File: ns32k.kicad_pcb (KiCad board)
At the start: 4 copper layers, 125.4 x 90.5 mm, 96 parts, among them J1 Conn_01x02_Pin, J2 3V3 Serial, J3 USB_C_USB2.0_16P, U1 NS32201, U10 74AHC373, U11 74AHC373, U12 74AHC138, U13 AS6C6416-55, U14 MT29F8G08ABACA, U15 MX29LV040C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

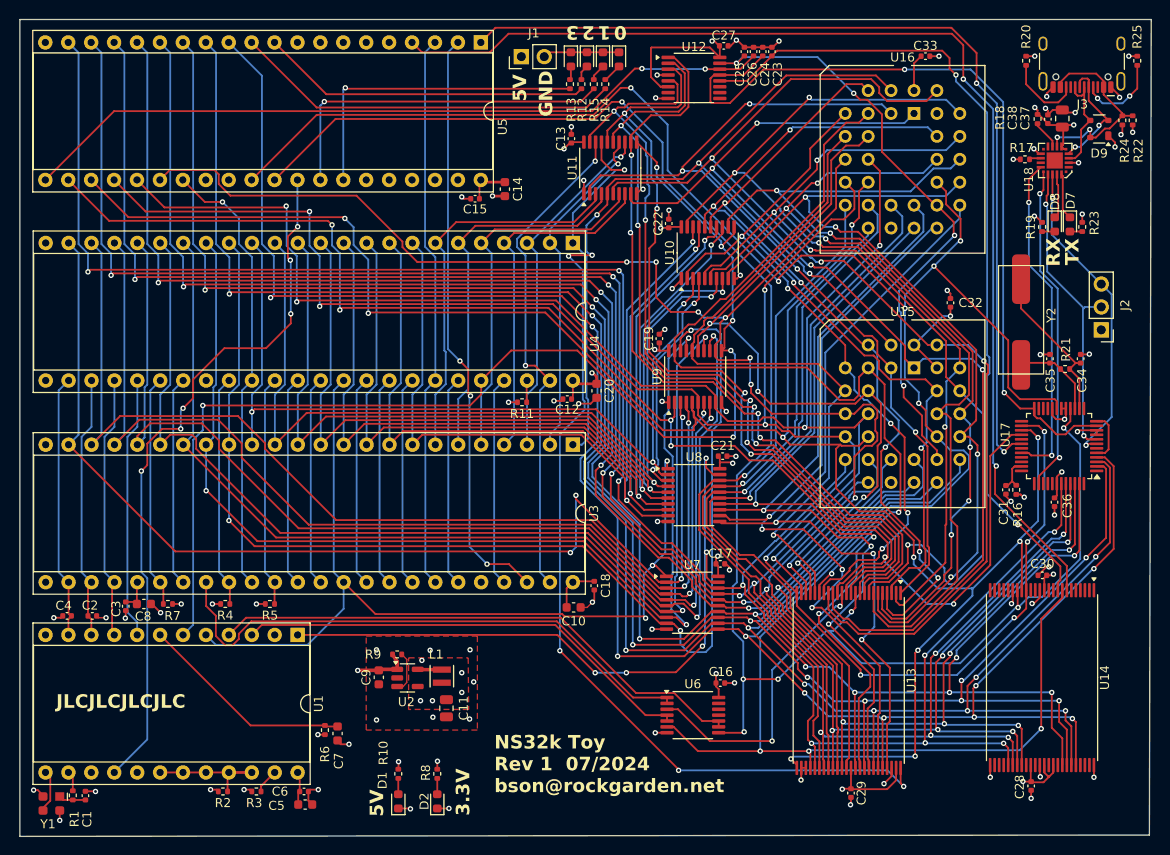
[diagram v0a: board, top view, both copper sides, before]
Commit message: add ICU int ack decoding
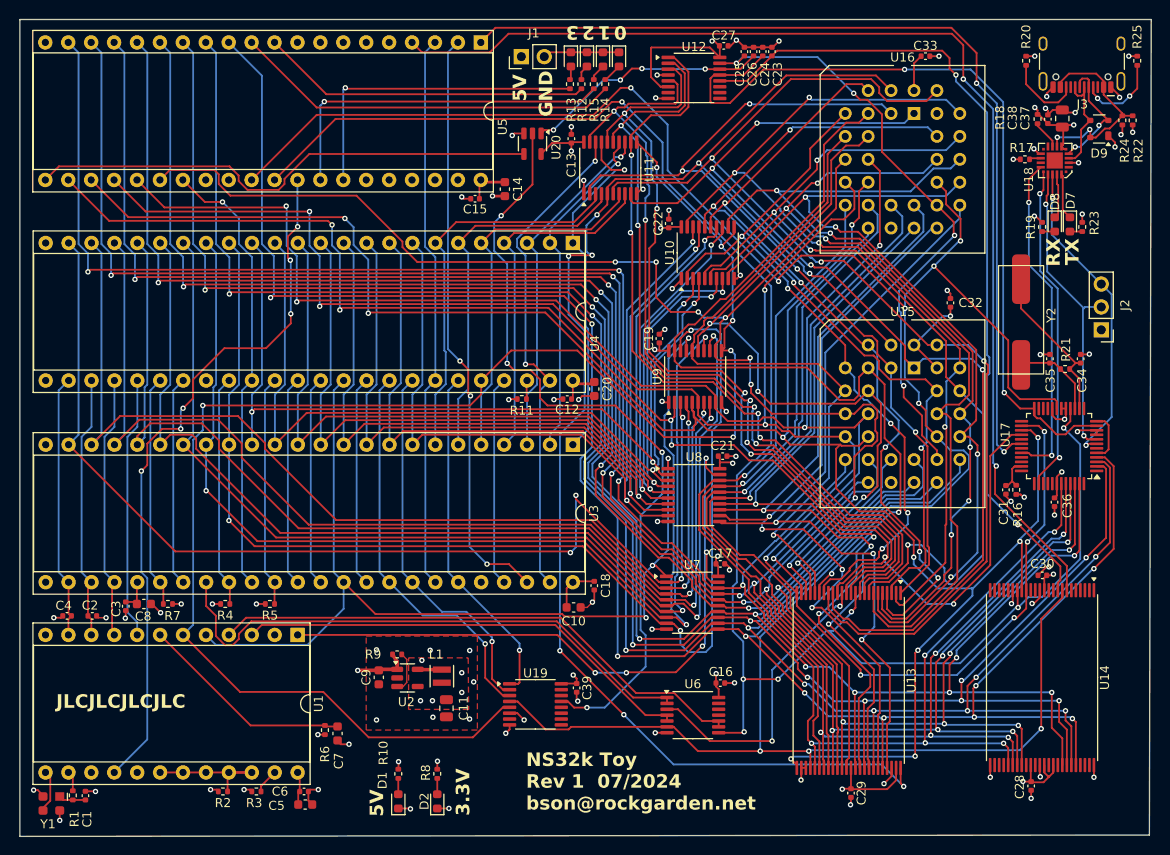
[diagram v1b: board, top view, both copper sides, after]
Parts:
- added C39: 0.1µF, Capacitor_SMD:C_0402_1005Metric, F.Cu at (113.4, 104.3)
- added U19: 74AHC138, Package_SO:TSSOP-16_4.4x5mm_P0.65mm, F.Cu at (108.8, 106.1)
- added U20: 74AHC1G08, Package_TO_SOT_SMD:SOT-23-5, F.Cu at (108.5, 44.0)
- U6: value 74LS08 -> 74AHC08
- moved R11 0.36 mm to (107.3, 72.3)
- moved C20 0.33 mm to (115.3, 71.2)
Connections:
- U5 pad 21: /~{ICU} -> Net-(U5B-~{CS})
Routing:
- net Net-(U19-O2): track 0.00 -> 86.8 mm, vias 0 -> 4
- net Net-(U5B-~{CS}): track 0.00 -> 57.1 mm
- net /~{ICU}: track 84.2 -> 27.2 mm, vias 2 -> 4
- net /~{PAV}: track 134.2 -> 176.5 mm
- net /ST3: track 23.3 -> 44.0 mm, vias 0 -> 1
- net /~{RD33}: track 260.8 -> 279.6 mm
- net /ST2: track 23.3 -> 41.7 mm, vias 0 -> 1
- net /ST0: track 23.3 -> 38.4 mm, vias 0 -> 1
- net +3V3: track 84.7 -> 93.2 mm, vias 26 -> 28
- net GND: track 92.9 -> 95.6 mm, vias 68 -> 71
- net +5V: track 33.2 -> 31.2 mm, vias 11 -> 10
- net /A22: track 40.4 -> 39.8 mm
- net /~{DDIN}: track 100.2 -> 100.8 mm

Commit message: move ICU# delay to after decode
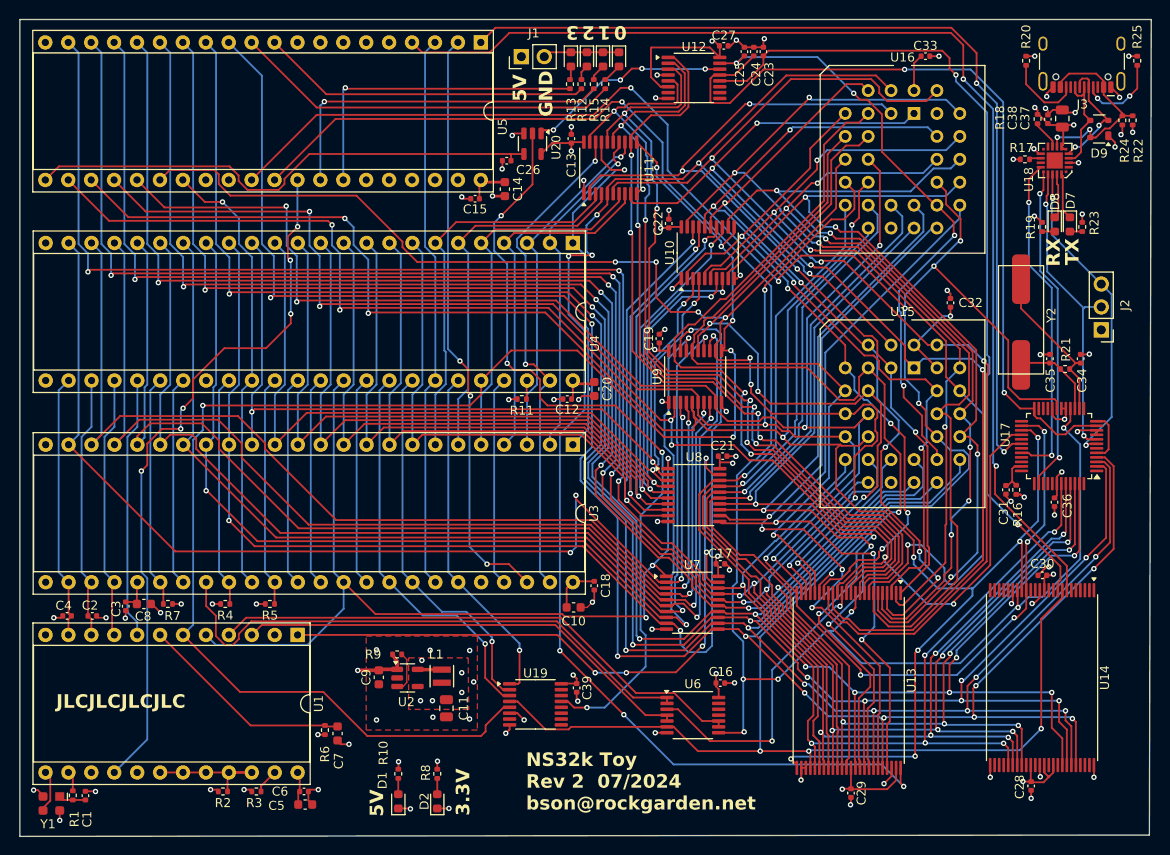
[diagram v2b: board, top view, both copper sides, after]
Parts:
- moved C26 29.9 mm to (105.6, 45.9), turned to 180 degrees
- moved C24 0.99 mm to (133.0, 33.8)
- moved C23 0.94 mm to (134.1, 33.8)
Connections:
- C26 pad 1: /~{ICU} -> Net-(U5B-~{CS})
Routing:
- net /~{ICU}: track 27.2 -> 22.8 mm
- net /~{SER_CS}: track 90.2 -> 89.2 mm
- net Net-(U5B-~{CS}): track 57.1 -> 57.9 mm
- net /~{NAND}: track 91.6 -> 92.2 mm
- net GND: vias 71 -> 72
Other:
- board text added: "NS32k Toy Rev 2 07/2024 bson@rockgarden.net"
- board text removed: "NS32k Toy Rev 1 07/2024 bson@rockgarden.net"

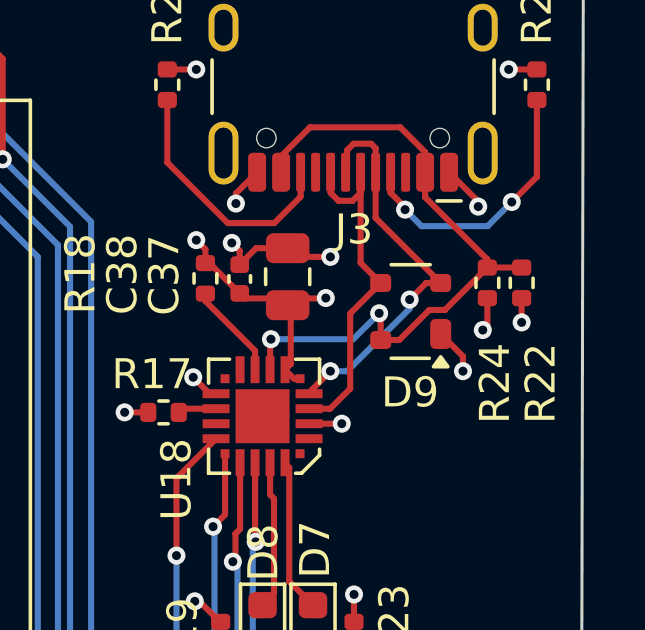
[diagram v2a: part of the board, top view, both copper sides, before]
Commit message: fix VUSB bug
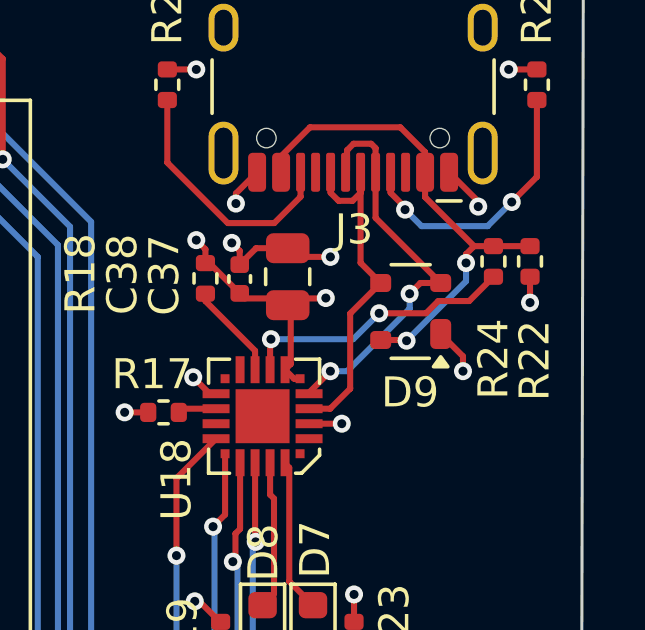
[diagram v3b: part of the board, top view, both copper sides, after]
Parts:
- R22: value 47k -> 47.5k
- R24: value 24k -> 22.1k
- moved R22 0.77 mm to (175.3, 40.7)
- moved R24 0.74 mm to (174.0, 40.7), turned to -90 degrees
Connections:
- D9 pad 4: Net-(U18-VBUS) -> Net-(D9-K-Pad4)
- J3 pad A4: Net-(U18-VBUS) -> Net-(D9-K-Pad4)
- J3 pad A9: Net-(U18-VBUS) -> Net-(D9-K-Pad4)
- J3 pad B4: Net-(U18-VBUS) -> Net-(D9-K-Pad4)
- J3 pad B9: Net-(U18-VBUS) -> Net-(D9-K-Pad4)
- R22 pad 1: Net-(U18-VBUS) -> Net-(D9-K-Pad4)
- R24 pad 1: +3V3 -> Net-(D9-K-Pad4)
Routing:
- net Net-(D9-K-Pad4): track 0.00 -> 16.2 mm, vias 0 -> 2
- net Net-(U18-VBUS): track 21.9 -> 9.31 mm
- net +3V3: track 93.2 -> 92.1 mm, vias 28 -> 27

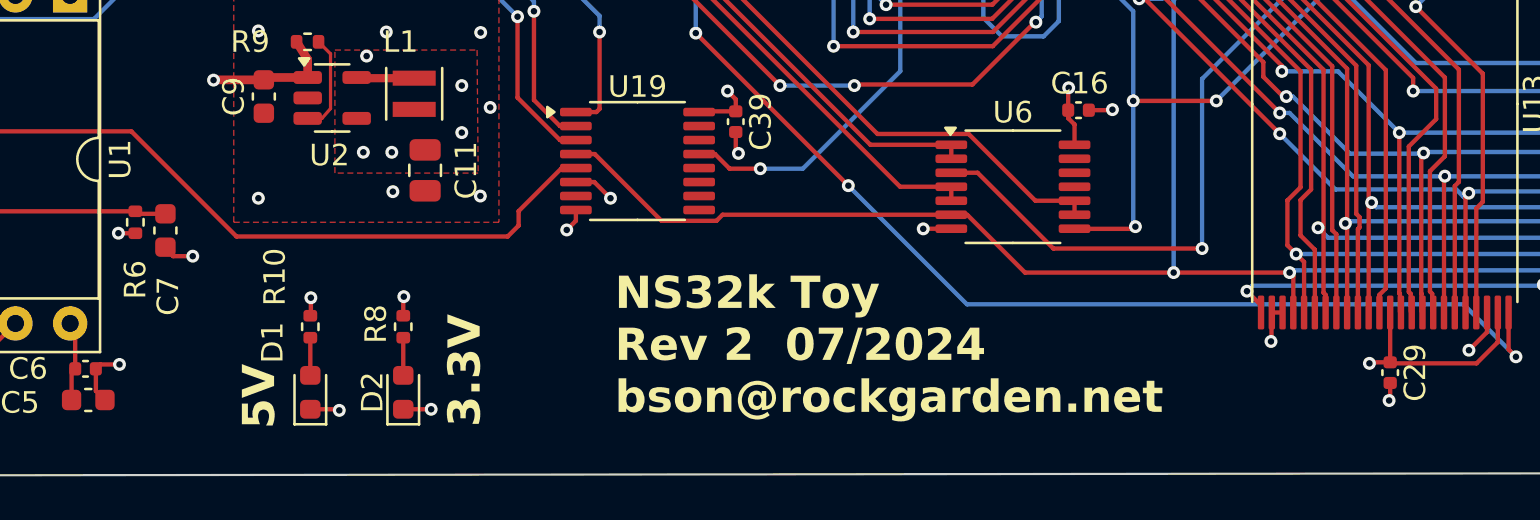
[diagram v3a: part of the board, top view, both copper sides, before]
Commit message: add reset button
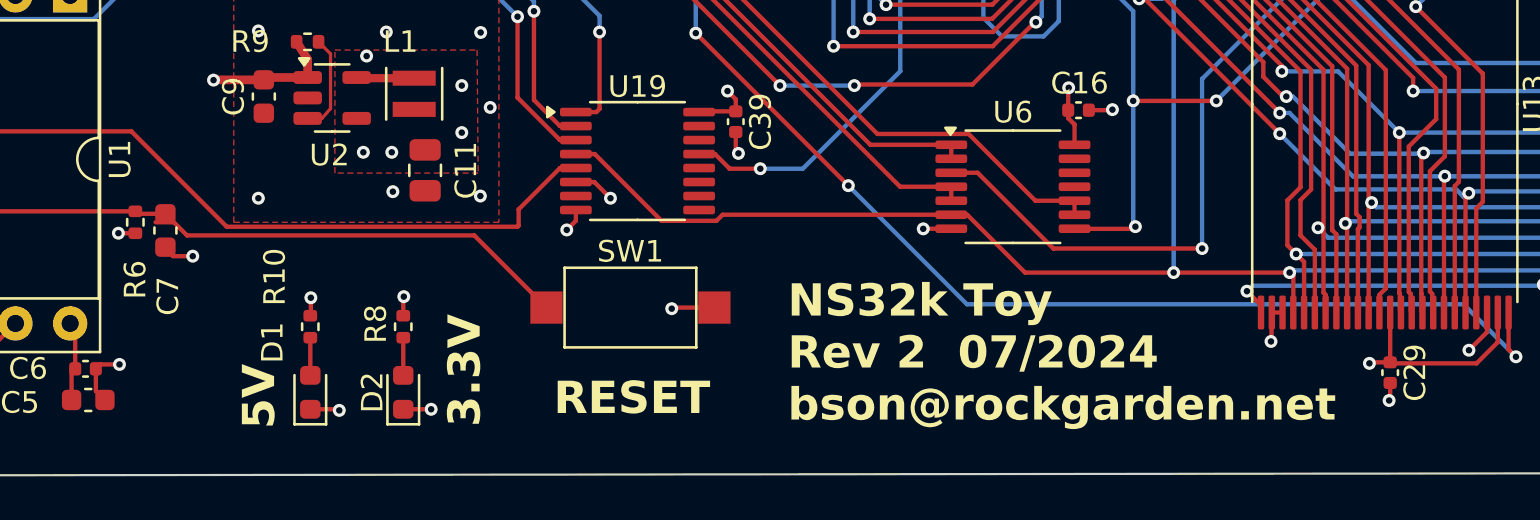
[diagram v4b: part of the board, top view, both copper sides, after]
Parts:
- added SW1: RESET, Button_Switch_SMD:SW_SPST_CK_RS282G05A3, F.Cu at (108.5, 112.9)
- J1: value Conn_01x02_Pin -> +5V SUPPLY
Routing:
- net Net-(U1B-~{RSTI}): track 23.7 -> 43.5 mm
- net GND: track 95.6 -> 97.6 mm, vias 72 -> 73
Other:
- board text added: "RESET"

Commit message: cleanups, DRC
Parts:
- added R26: 30k, Resistor_SMD:R_0402_1005Metric, B.Cu at (84.4, 35.9)
- added R27: 30k, Resistor_SMD:R_0402_1005Metric, F.Cu at (92.5, 50.5)
- added R28: 30k, Resistor_SMD:R_0402_1005Metric, B.Cu at (87.6, 35.9)
- added R29: 30k, Resistor_SMD:R_0402_1005Metric, F.Cu at (95.2, 50.5)
- added SW2: SW_DIP_x04, Button_Switch_SMD:SW_DIP_SPSTx04_Slide_Copal_CHS-04B_W7.62mm_P1.27mm, B.Cu at (75.9, 40.8)
- J3, R20, R25: moved to B.Cu
- moved R20 12.4 mm to (175.4, 37.2)
- moved R25 12.4 mm to (163.3, 37.2)
- moved Y1 5.48 mm to (54.7, 111.6), turned to 90 degrees
- moved C7 4.87 mm to (91.2, 111.6)
- moved R6 4.87 mm to (89.8, 111.2)
- moved U1 3.94 mm to (86.4, 98.4)
- moved D1 3.91 mm to (95.2, 113.3), turned to -90 degrees
- moved D2 3.90 mm to (99.5, 113.3), turned to -90 degrees
- moved C6 3.70 mm to (86.9, 115.9)
- moved C1 3.43 mm to (55.6, 115.4), turned to 0 degrees
- moved R1 2.90 mm to (55.6, 114.0), turned to 0 degrees
- moved C5 1.28 mm to (84.0, 116.2), turned to 180 degrees
- moved C29 1.25 mm to (143.3, 114.8), turned to 180 degrees
- moved C2 0.88 mm to (60.5, 96.0)
- moved D9 0.83 mm to (170.8, 41.7), turned to -90 degrees
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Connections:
- U5 pad 35: unconnected-(U5B-IR5-Pad35) -> Net-(U5B-IR5)
- U5 pad 36: unconnected-(U5B-IR7-Pad36) -> Net-(U5B-IR7)
- U5 pad 8: unconnected-(U5B-IR6-Pad8) -> Net-(U5B-IR6)
- U5 pad 9: unconnected-(U5B-IR4-Pad9) -> Net-(U5B-IR4)
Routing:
- net Net-(U5B-IR5): track 0.00 -> 20.6 mm
- net Net-(U5B-IR6): track 0.00 -> 20.5 mm
- net Net-(U5B-IR7): track 0.00 -> 18.4 mm, vias 0 -> 1
- net GND: track 97.6 -> 115.0 mm, vias 73 -> 77
- net Net-(U5B-IR4): track 0.00 -> 11.0 mm
- net +5V: track 31.2 -> 39.9 mm, vias 10 -> 12
- net /~{DDIN}: track 100.8 -> 94.2 mm
- net Net-(U1B-~{RSTI}): track 43.5 -> 39.3 mm
- net Net-(U1B-XOUT): track 1.54 -> 5.60 mm
- net /~{DBE}: track 76.2 -> 72.2 mm
- net /~{RD}: track 51.3 -> 47.4 mm
- net /~{WR}: track 60.5 -> 56.7 mm, vias 0 -> 1
- net /~{HBE}: track 62.4 -> 58.7 mm
- net /~{PER}: track 2.74 -> 6.34 mm
- net /~{PAV}: track 176.4 -> 173.2 mm
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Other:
- board size 125.4 x 90.5 mm -> 125.5 x 88.3 mm
- board text added: "A"
- board text added: "B"
- board text added: "C"
- board text added: "D"
